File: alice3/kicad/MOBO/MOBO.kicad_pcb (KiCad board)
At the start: 2 copper layers, 97.8 x 114.3 mm, 40 parts, among them CON1 SD_Card, SW1 RESET, SW2 SOFT RESET, SW3 POWER, U1 LM2937-3.3, U2 VGA_daughter_board, U3 Propeller_P8X32A-D40, U4 24LC256, U5 Propeller_Plug, U6 MiniM4-D40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

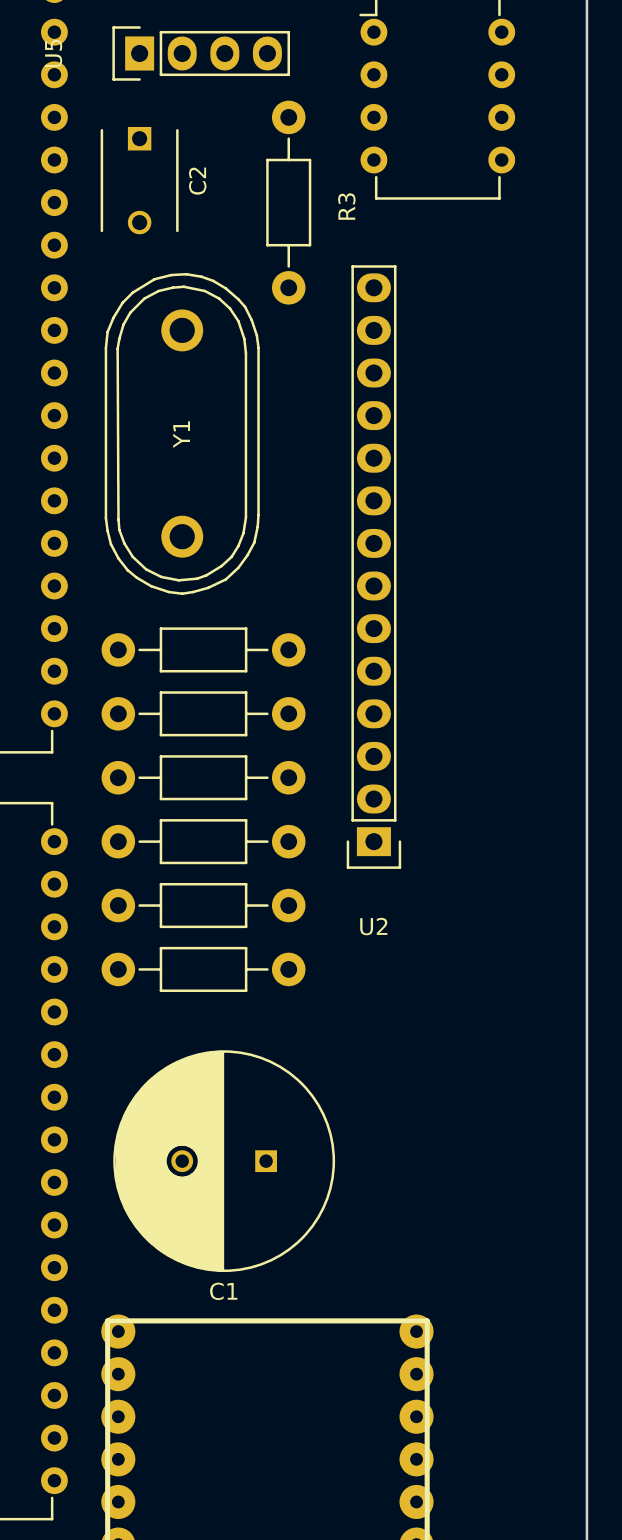
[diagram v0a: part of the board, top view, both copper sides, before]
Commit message: Add breakout header for 3 more prop pins.
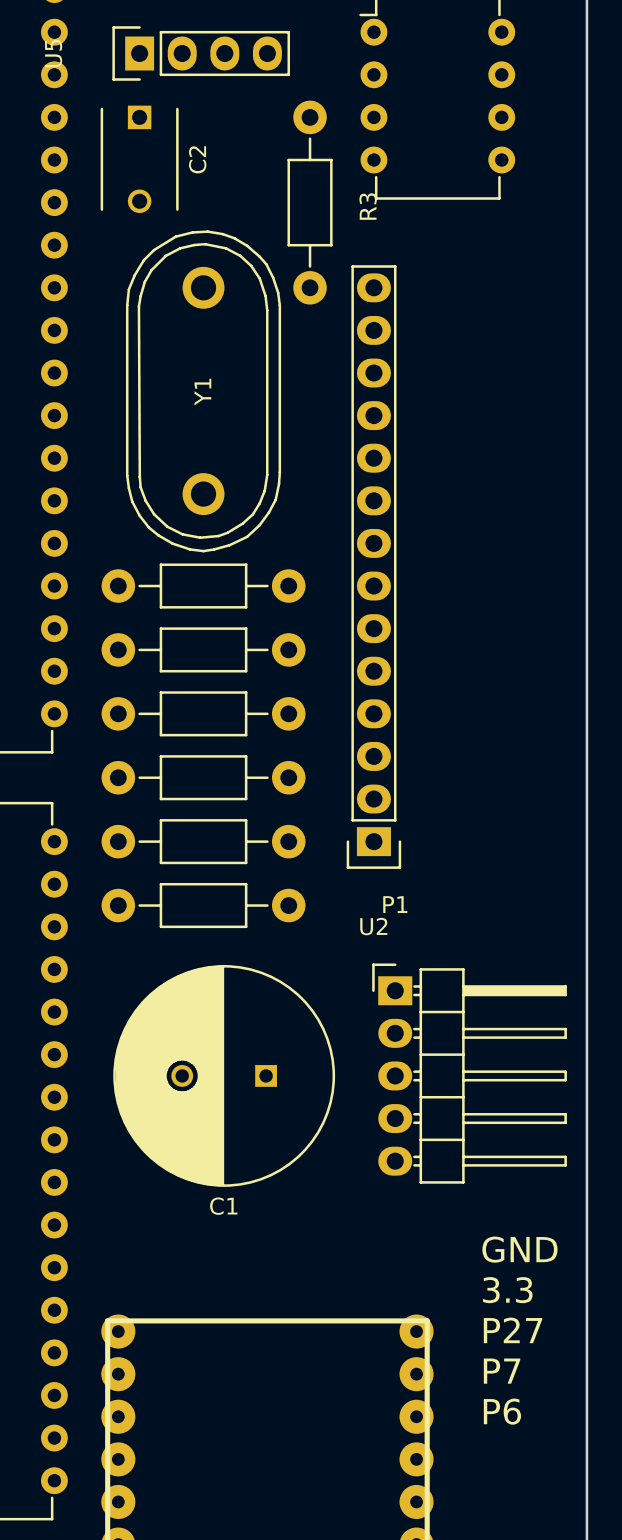
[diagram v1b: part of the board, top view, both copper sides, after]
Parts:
- added P1: GPIO, Pin_Headers:Pin_Header_Angled_1x05, F.Cu at (132.1, 104.1)
- moved C1 5.08 mm to (124.4, 109.2)
- moved R11 3.81 mm to (120.7, 99.1)
- moved R12 3.81 mm to (120.7, 95.2)
- moved R13 3.81 mm to (120.7, 87.6)
- moved R14 3.81 mm to (120.7, 91.4)
- moved R15 3.81 mm to (120.7, 83.8)
- moved R16 3.81 mm to (120.7, 80.0)
- moved Y1 2.84 mm to (120.7, 68.4)
- moved C2 1.27 mm to (116.8, 52.1)
- moved R3 1.27 mm to (127.0, 57.1)
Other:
- board text added: "GND 3.3 P27 P7 P6"

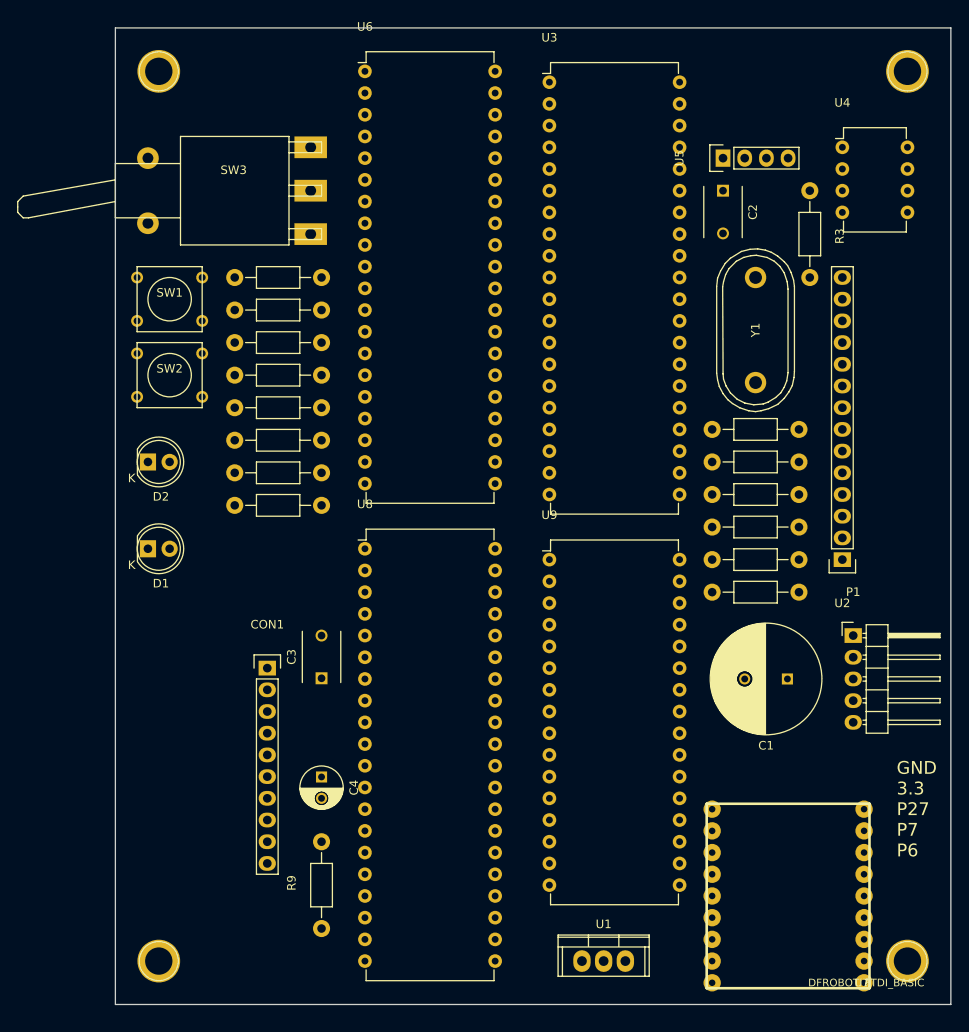
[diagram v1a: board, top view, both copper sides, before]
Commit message: Remove on/off switch.
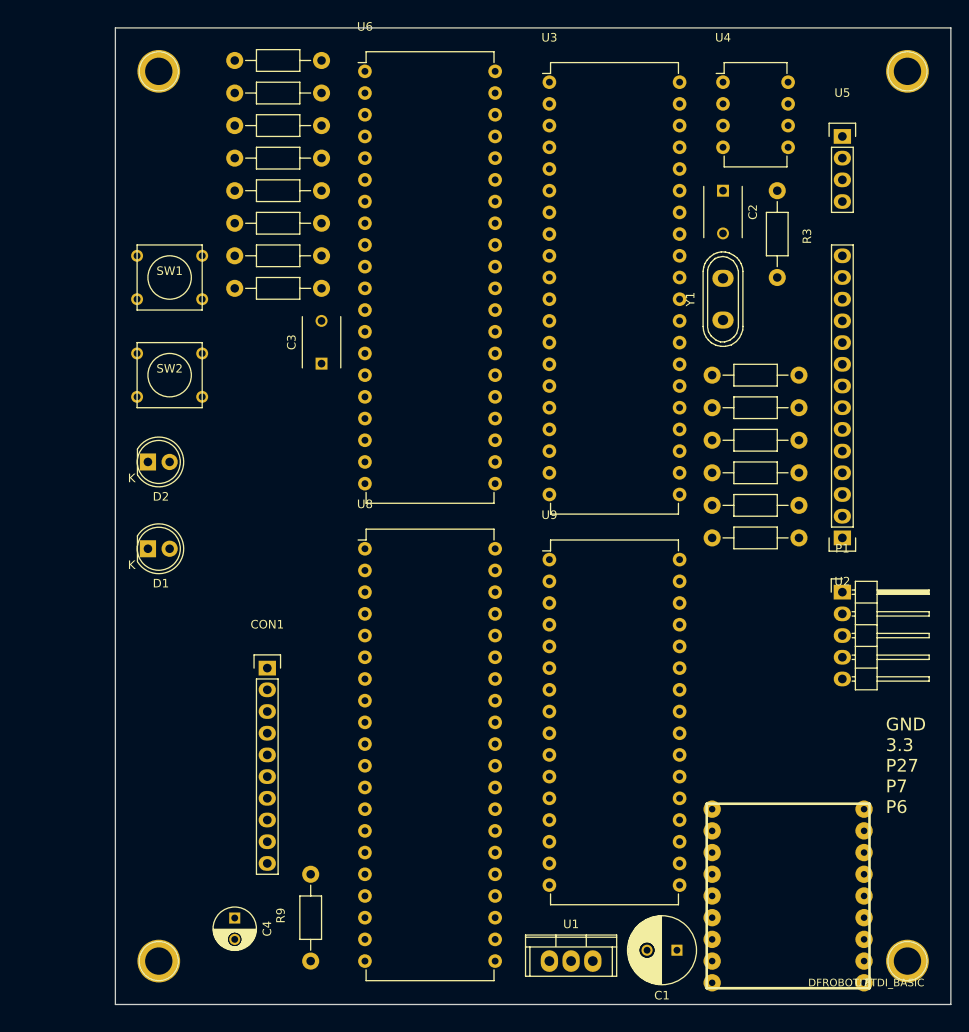
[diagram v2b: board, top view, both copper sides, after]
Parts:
- removed SW3: POWER, Buttons_Switches_ThroughHole:SW_SPDT
- C1: footprint Capacitors_ThroughHole:C_Radial_D13_L21_P5 -> Capacitors_ThroughHole:C_Radial_D8_L11.5_P3.5
- P1: value GPIO -> CONN_01X05
- Y1: footprint Crystals:Crystal_HC48-U_Vertical -> Crystals:Crystal_HC50-U_Vertical
- moved C3 36.8 mm to (69.8, 72.3)
- moved C1 34.3 mm to (111.5, 141.0)
- moved R1 25.4 mm to (64.8, 59.7)
- moved R7 25.4 mm to (64.8, 63.5)
- moved R8 25.4 mm to (64.8, 40.6)
- moved R10 25.4 mm to (64.8, 36.8)
- moved R4 25.4 mm to (64.8, 55.9)
- moved R5 25.4 mm to (64.8, 48.3)
- moved R6 25.4 mm to (64.8, 52.1)
- moved R2 25.4 mm to (64.8, 44.5)
- moved C4 19.4 mm to (59.7, 137.2)
- moved U4 15.9 mm to (116.8, 39.4)
- moved U5 14.2 mm to (130.8, 45.7), turned to 0 degrees
- moved R11 6.35 mm to (120.7, 92.7)
- moved R16 6.35 mm to (120.7, 73.7)
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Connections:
- U7 pad 13: Net-(SW3-Pad1) -> +5V

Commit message: Before removing DFROBOT.
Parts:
- added C5: 0.1 µF, Capacitors_ThroughHole:C_Disc_D6_P5, F.Cu at (104.1, 102.9)
- C3: value 0.1µ -> 22µF; footprint Capacitors_ThroughHole:C_Disc_D6_P5 -> Capacitors_ThroughHole:C_Radial_D5_L11_P2.5
- C4: value 22µF -> 0.1 µF; footprint Capacitors_ThroughHole:C_Radial_D5_L11_P2.5 -> Capacitors_ThroughHole:C_Disc_D6_P5
- moved C3 46.3 mm to (57.1, 116.8)
- moved C4 15.5 mm to (57.1, 121.9)
- moved R16 14.8 mm to (108.0, 81.3)
- moved R15 14.2 mm to (108.0, 83.8)
- moved R13 13.7 mm to (108.0, 86.4)
- moved CON1 13.3 mm to (50.8, 104.1)
- moved R14 13.3 mm to (108.0, 88.9)
- moved R10 13.1 mm to (53.3, 43.2)
- moved R12 13.0 mm to (108.0, 91.4)
- moved R11 12.8 mm to (108.0, 94.0)
- moved U3 12.8 mm to (83.8, 38.1)
- moved U9 12.8 mm to (83.8, 94.0)
- moved U6 12.7 mm to (62.2, 38.1)
- moved U8 12.7 mm to (62.2, 94.0)
- moved C1 12.7 mm to (98.8, 141.0)
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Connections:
- C4 pad 1: +3V3 -> +5V
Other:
- board size 97.8 x 114.3 mm -> 85.1 x 114.3 mm

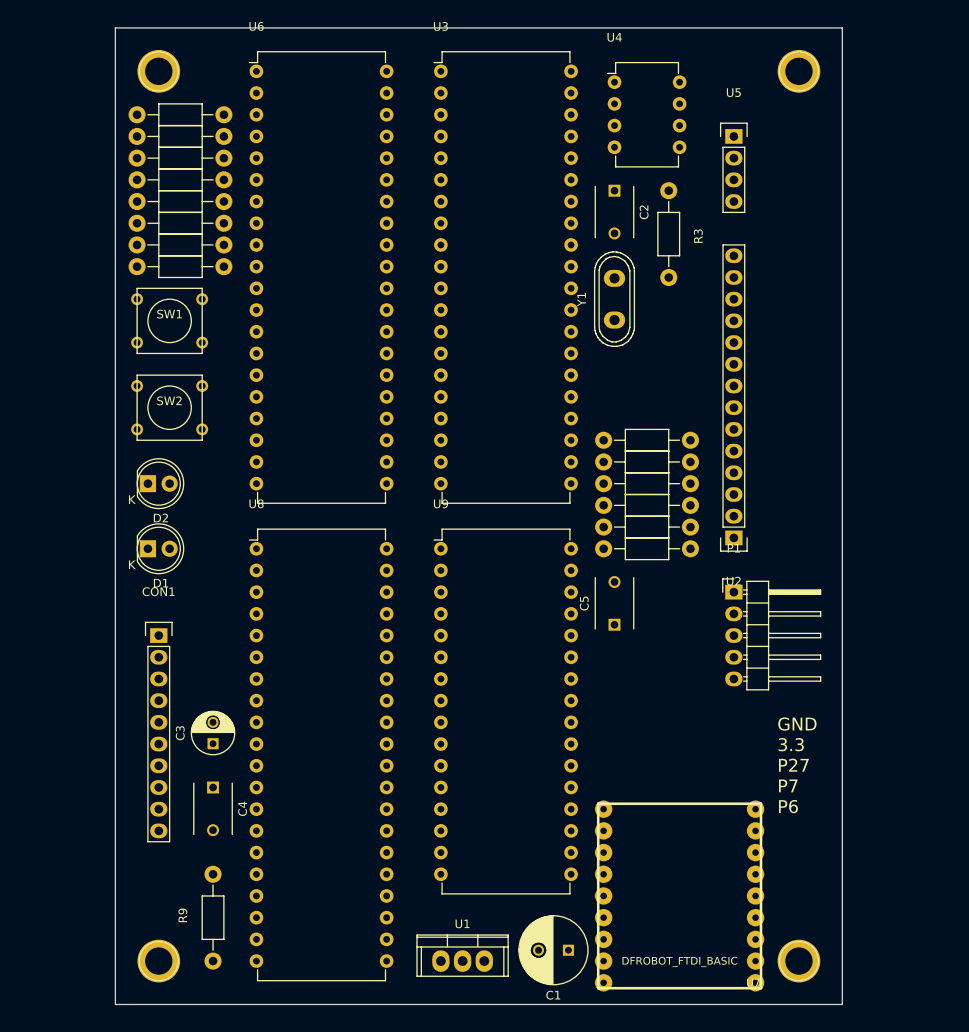
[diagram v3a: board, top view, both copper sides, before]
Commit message: Remove DFROBOT and LDO.
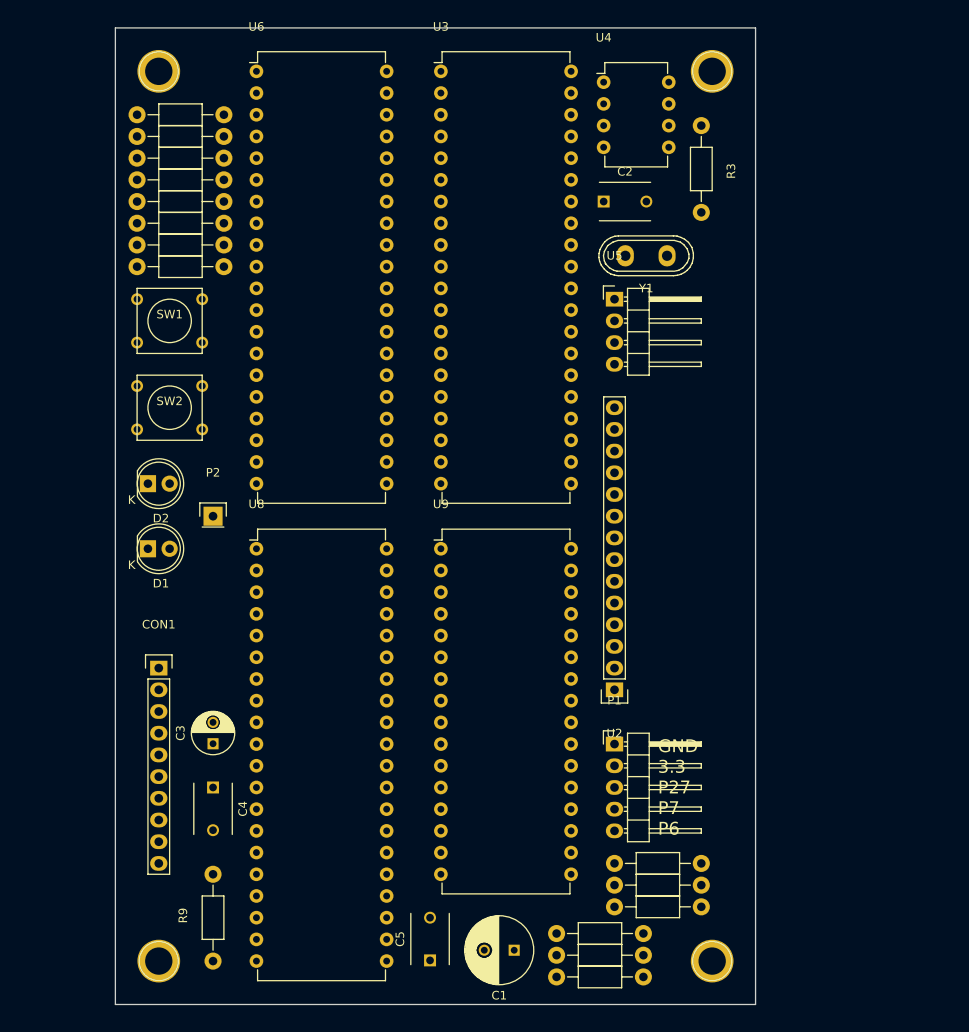
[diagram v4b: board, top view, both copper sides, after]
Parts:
- removed U1: LM2937-3.3, Power_Integrations:TO-220
- removed U7: DFROBOT_FTDI_BASIC, ftdi basic breakout:FTDIBASIC
- added P2: CONN_01X01, Pin_Headers:Pin_Header_Straight_1x01, F.Cu at (57.1, 90.2)
- U5: footprint Pin_Headers:Pin_Header_Straight_1x04 -> Pin_Headers:Pin_Header_Angled_1x04
- moved R12 50.4 mm to (102.4, 141.6)
- moved R14 50.4 mm to (102.4, 139.0)
- moved R11 50.4 mm to (102.4, 144.1)
- moved R15 49.5 mm to (109.2, 133.3)
- moved R16 49.5 mm to (109.2, 130.8)
- moved R13 49.5 mm to (109.2, 135.9)
- moved C5 44.8 mm to (82.5, 142.2)
- moved U5 23.6 mm to (104.1, 64.8)
- moved P1 22.6 mm to (104.1, 116.8)
- moved U2 22.6 mm to (104.1, 110.5)
- moved REF** 10.2 mm to (115.6, 142.2)
- moved REF** 10.2 mm to (115.6, 38.1)
- moved R3 8.52 mm to (114.3, 49.5)
- moved C1 6.35 mm to (92.4, 141.0)
- moved Y1 6.29 mm to (107.9, 59.7), turned to 180 degrees
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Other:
- board size 85.1 x 114.3 mm -> 74.9 x 114.3 mm

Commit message: FreeRoute PCB layout
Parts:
- renumbered REF** to HOLE1, REF** to HOLE2, REF** to HOLE3, REF** to HOLE4
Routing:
- net +3V3: track 0.00 -> 285.6 mm, vias 0 -> 2
- net +5V: track 0.00 -> 198.4 mm, vias 0 -> 1
- net /RD: track 0.00 -> 178.1 mm
- net D7: track 0.00 -> 174.4 mm, vias 0 -> 1
- net D3: track 0.00 -> 156.7 mm, vias 0 -> 4
- net D6: track 0.00 -> 152.2 mm
- net D0: track 0.00 -> 149.1 mm, vias 0 -> 1
- net D2: track 0.00 -> 146.4 mm, vias 0 -> 1
- net D1: track 0.00 -> 146.4 mm, vias 0 -> 2
- net D5: track 0.00 -> 145.9 mm
- net D4: track 0.00 -> 145.4 mm, vias 0 -> 2
- net /WR: track 0.00 -> 144.9 mm, vias 0 -> 2
- net /IO/DO: track 0.00 -> 135.6 mm
- net /IORQ: track 0.00 -> 121.6 mm
- net A0: track 0.00 -> 119.5 mm
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- added copper zone on B.Cu, net GND

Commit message: Alice 3 v1 schematic and PCB, sent to OSHPark
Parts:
- C3: value 22µF -> 10µF
- moved C5 3.73 mm to (82.5, 138.4), turned to 270 degrees
- moved C3 2.50 mm to (57.1, 114.3), turned to 270 degrees
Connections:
- C4 pad 1: +5V -> +3V3
- C5 pad 1: +5V -> +3V3
- HOLE1 pad 1: (no net) -> GND
- HOLE2 pad 1: (no net) -> GND
- HOLE3 pad 1: (no net) -> GND
- HOLE4 pad 1: (no net) -> GND
- R10 pad 1: +5V -> +3V3
- U8 pad 11: +5V -> +3V3
- U8 pad 16: +5V -> +3V3
- U8 pad 17: +5V -> +3V3
- U8 pad 24: +5V -> +3V3
- U9 pad 30: +5V -> +3V3
- U9 pad 32: VCC -> +3V3
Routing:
- net +3V3: track 285.6 -> 65.1 mm, vias 2 -> 0
- net +5V: track 198.4 -> 73.4 mm, vias 1 -> 4
- net D5: track 145.9 -> 191.6 mm, vias 0 -> 1
- net /IORQ: track 121.6 -> 163.0 mm
- net A14: track 67.9 -> 107.5 mm
- net /RD: track 178.1 -> 147.9 mm, vias 0 -> 3
- net D0: track 149.1 -> 177.5 mm, vias 1 -> 0
- net D4: track 145.4 -> 169.5 mm
- net A5: track 78.0 -> 53.9 mm, vias 0 -> 2
- net A9: track 79.0 -> 57.4 mm, vias 1 -> 0
- net /IO/DO: track 135.6 -> 114.2 mm
- net A15: track 76.0 -> 94.2 mm
- net /MREQ: track 110.4 -> 94.3 mm
- net CLK: track 70.7 -> 82.7 mm
- net /IO/DI: track 96.2 -> 85.6 mm, vias 1 -> 2
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- added copper zone on F.Cu, net +3V3
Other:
- board text added: "A>_"
- board text added: "Alice 3 Z80/Propeller/ARM v1 lawrence.kesteloot@gmail.com grantham@plunk.org lkesteloot.github.io/alice/alice3/"
- board text added: "Alice 3 v1 2016 BG & LK"
- board text added: "BARTCONN"
- board text added: "HARD"
- board text added: "SOFT"
